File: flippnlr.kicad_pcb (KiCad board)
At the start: 2 copper layers, 87 parts, among them J1 Pwr In, J2 TP3, J3 TP1, J4 Opt Out, J5 Opt Out, J6 Data Out, J7 Data In, J8 TP2, U1 LD1117 3.3V, U10 TPL7407LA, U11 TPL7407LA, U12 TPL7407LA, U13 SN74HCS365, U2 SN74HCS594, U3 SN74HCS594, U4 SN74HCS594, U5 SN74HCS594, U6 SN74HCS594, U7 TPL7407LA, U8 TPL7407LA, U9 TPL7407LA

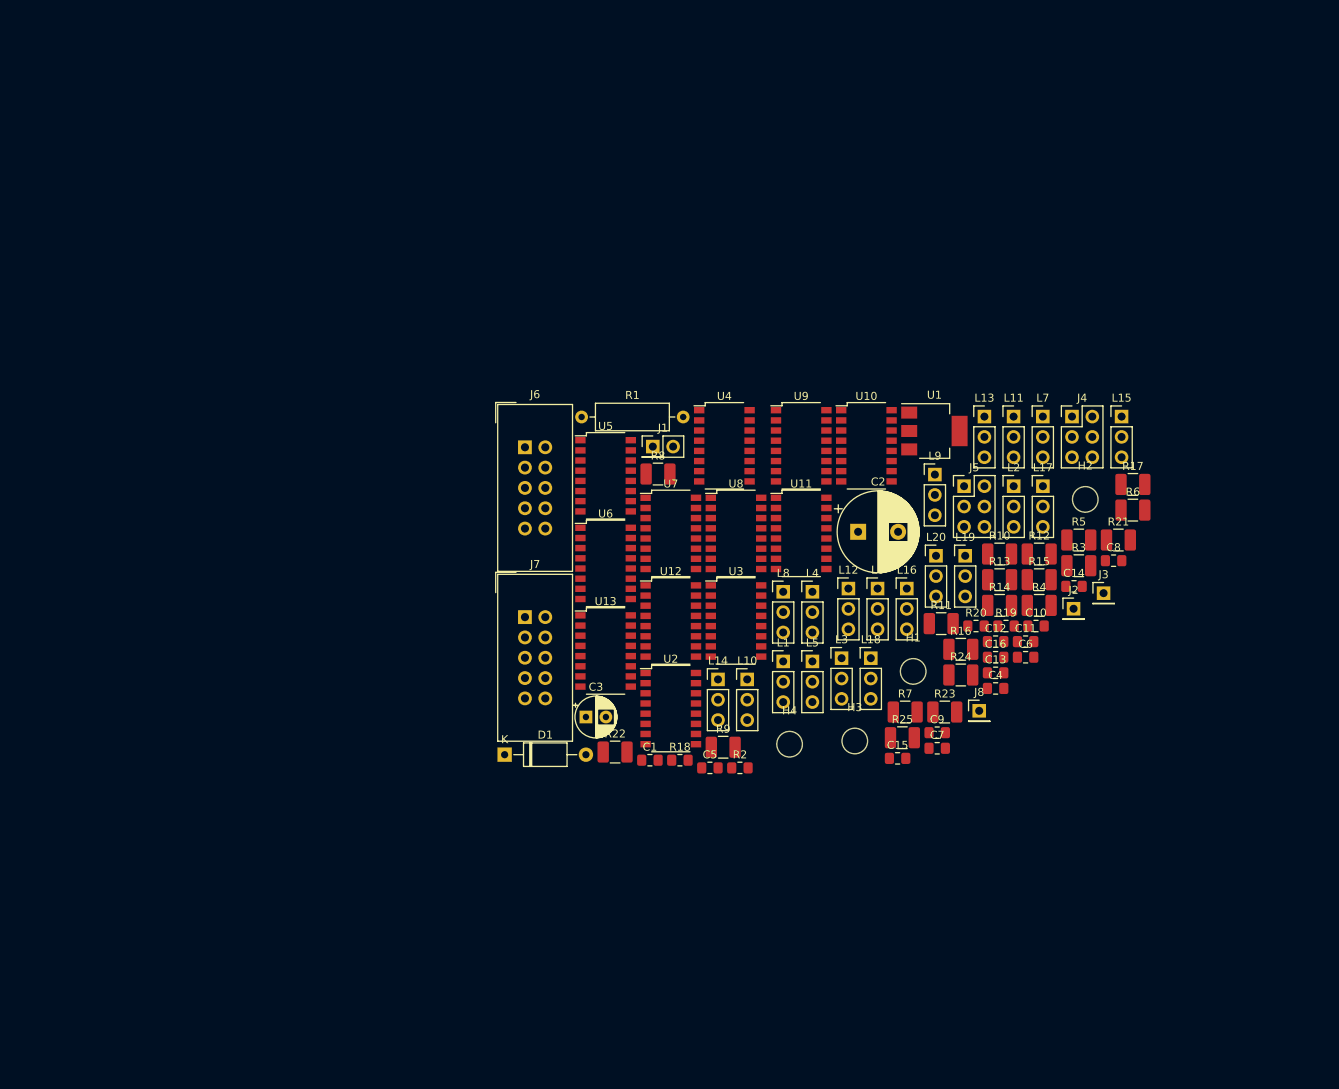
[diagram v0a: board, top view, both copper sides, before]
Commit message: fix kicad lib path and begin layout
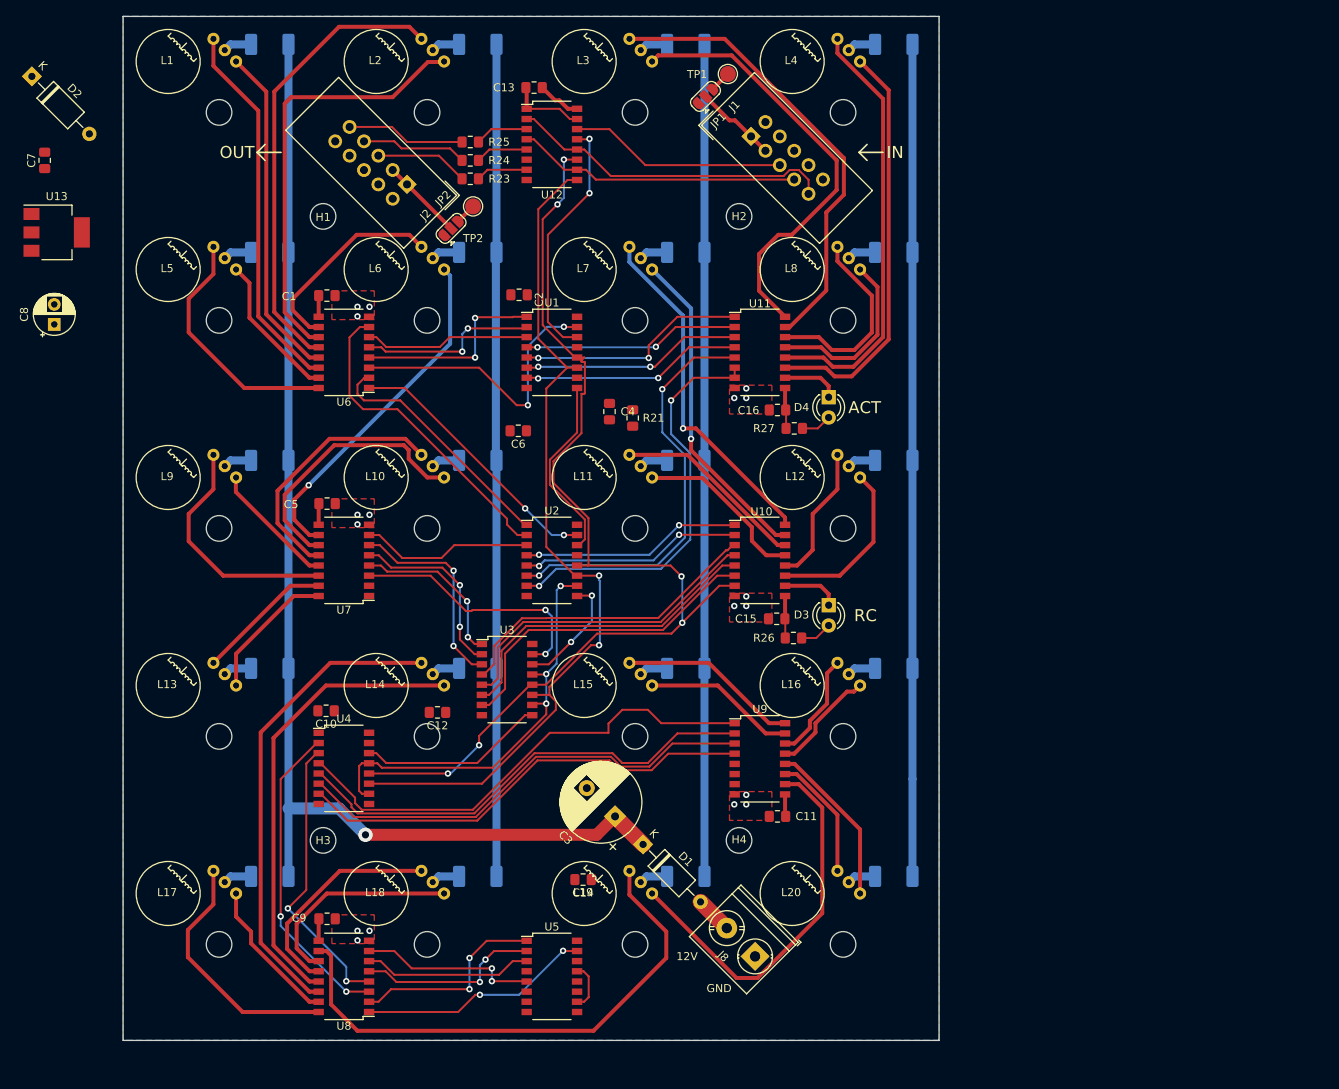
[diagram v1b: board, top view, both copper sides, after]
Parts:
- removed J3: TP1, Connector_PinHeader_2.54mm:PinHeader_1x01_P2.54mm_Vertical
- removed J4, J5: Opt Out, Connector_PinHeader_2.54mm:PinHeader_2x03_P2.54mm_Vertical
- removed J6: Data Out, Connector_IDC:IDC-Header_2x05_P2.54mm_Vertical
- removed J7: Data In, Connector_IDC:IDC-Header_2x05_P2.54mm_Vertical
- removed R22: TBA, Resistor_SMD:R_1210_3225Metric_Pad1.42x2.65mm_HandSolder
- added D2: 1n5817, Diode_THT:D_A-405_P10.16mm_Horizontal, F.Cu at (38.6, 35.5)
- added D3: 3GWY4, LED_THT:LED_D3.0mm, F.Cu at (138.2, 101.6)
- added D4: 3GWY4, LED_THT:LED_D3.0mm, F.Cu at (138.2, 75.6)
- added JP1: PWR, Jumper:SolderJumper-3_P1.3mm_Open_RoundedPad1.0x1.5mm, F.Cu at (122.8, 38.0)
- added JP2: PWR, Jumper:SolderJumper-3_P1.3mm_Open_RoundedPad1.0x1.5mm, F.Cu at (91.0, 54.5)
- added R26: 4k7, Resistor_SMD:R_0805_2012Metric_Pad1.15x1.40mm_HandSolder, F.Cu at (133.8, 105.7)
- added R27: 4k7, Resistor_SMD:R_0805_2012Metric_Pad1.15x1.40mm_HandSolder, F.Cu at (133.9, 79.5)
- added TP1: PWR, TestPoint:TestPoint_Pad_D2.0mm, F.Cu at (125.6, 35.2)
- added TP2: PWR, TestPoint:TestPoint_Pad_D2.0mm, F.Cu at (93.8, 51.8)
- C2: value 470uF -> 100nF; footprint Capacitor_THT:CP_Radial_D10.0mm_P5.00mm -> Capacitor_SMD:C_0805_2012Metric_Pad1.15x1.40mm_HandSolder
- C3: value 10uF -> 470uF; footprint Capacitor_THT:CP_Radial_D5.0mm_P2.50mm -> Capacitor_THT:CP_Radial_D10.0mm_P5.00mm
- C8: value 100nF -> 10uF; footprint Capacitor_SMD:C_0805_2012Metric_Pad1.15x1.40mm_HandSolder -> Capacitor_THT:CP_Radial_D5.0mm_P2.50mm
- D1: value 1n4001 -> 1n5817
- J1: value Pwr In -> Data In; footprint Connector_PinHeader_2.54mm:PinHeader_2x01_P2.54mm_Vertical -> Connector_IDC:IDC-Header_2x05_P2.54mm_Vertical
- J2: value TP3 -> Data Out; footprint Connector_PinHeader_2.54mm:PinHeader_1x01_P2.54mm_Vertical -> Connector_IDC:IDC-Header_2x05_P2.54mm_Vertical
- J8: value TP2 -> 12V; footprint Connector_PinHeader_2.54mm:PinHeader_1x01_P2.54mm_Vertical -> TerminalBlock_Phoenix:TerminalBlock_Phoenix_PT-1,5-2-5.0-H_1x02_P5.00mm_Horizontal
- L1, L10, L11, L12, L13, L14, L15, L16, L17, L18, L19, L2, L20, L3, L4, L5, L6, L7, L8, L9: footprint Connector_PinHeader_2.54mm:PinHeader_1x03_P2.54mm_Vertical -> flipdot:Flipdot
- R1: value 2.7 -> 62; footprint Resistor_THT:R_Axial_DIN0309_L9.0mm_D3.2mm_P12.70mm_Horizontal -> Resistor_SMD:R_2010_5025Metric_Pad1.52x2.65mm_HandSolder; moved to B.Cu
- R10, R11, R12, R13, R14, R15, R16, R17, R3, R4, R5, R6, R7, R8, R9: value TBA -> 62; footprint Resistor_SMD:R_1210_3225Metric_Pad1.42x2.65mm_HandSolder -> Resistor_SMD:R_2010_5025Metric_Pad1.52x2.65mm_HandSolder; moved to B.Cu
- R18, R19, R20: value 33 -> 62; footprint Resistor_SMD:R_0805_2012Metric_Pad1.15x1.40mm_HandSolder -> Resistor_SMD:R_2010_5025Metric_Pad1.52x2.65mm_HandSolder; moved to B.Cu
- R2: value 1k -> 62; footprint Resistor_SMD:R_0805_2012Metric_Pad1.15x1.40mm_HandSolder -> Resistor_SMD:R_2010_5025Metric_Pad1.52x2.65mm_HandSolder; moved to B.Cu
- R21: value TBA -> 1k; footprint Resistor_SMD:R_1210_3225Metric_Pad1.42x2.65mm_HandSolder -> Resistor_SMD:R_0805_2012Metric_Pad1.15x1.40mm_HandSolder
- R23, R24, R25: value TBA -> 33; footprint Resistor_SMD:R_1210_3225Metric_Pad1.42x2.65mm_HandSolder -> Resistor_SMD:R_0805_2012Metric_Pad1.15x1.40mm_HandSolder
- U1: value LD1117 3.3V -> SN74HCS594; footprint Package_TO_SOT_SMD:SOT-223-3_TabPin2 -> Package_SO:SOP-16_4.4x10.4mm_P1.27mm
- U12: value TPL7407LA -> SN74HCS365
- U13: value SN74HCS365 -> LD1117 3.3V; footprint Package_SO:SOP-16_4.4x10.4mm_P1.27mm -> Package_TO_SOT_SMD:SOT-223-3_TabPin2
- U6: value SN74HCS594 -> TPL7407LA
- moved C8 135.7 mm to (41.4, 66.5), turned to 90 degrees
- moved C7 133.6 mm to (40.2, 46.0), turned to 90 degrees
- moved R17 118.5 mm to (68.3, 135.5)
- moved L17 117.8 mm to (62.0, 144.0), turned to 315 degrees
- moved R5 107.3 mm to (68.3, 57.5)
- moved L13 103.7 mm to (62.0, 118.0), turned to 315 degrees
- moved J2 98.8 mm to (85.5, 49.0), turned to 225 degrees
- moved L1 98.4 mm to (62.0, 40.0), turned to 315 degrees
- moved R2 96.2 mm to (94.3, 31.5)
- moved C13 93.2 mm to (101.4, 36.9), turned to 180 degrees
- moved H1 93.1 mm to (75.0, 53.0)
- moved R25 92.0 mm to (93.4, 43.7)
- moved R13 91.9 mm to (68.3, 109.5)
- moved L9 89.7 mm to (62.0, 92.0), turned to 315 degrees
- moved C10 89.4 mm to (75.4, 114.8), turned to 180 degrees
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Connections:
- C1 pad 1: +10V -> +12V
- C10 pad 1: +12V -> +3V3
- C12 pad 1: +12V -> +3V3
- C13 pad 1: +12V -> +3V3
- C14 pad 1: +12V -> +3V3
- C16 pad 1: +3V3 -> +12V
- C2 pad 1: +12V -> +3V3
- C3 pad 1: +3V3 -> +12V
- C4 pad 1: +3V3 -> GND
- C4 pad 2: GND -> RST
- C5 pad 1: +3V3 -> +12V
- C7 pad 1: +3V3 -> +10V
- C9 pad 1: GND -> +12V
- C9 pad 2: RST -> GND
- D1 pad 1: +10V -> +12V
- D1 pad 2: +12V -> Net-(D1-Pad2)
- J8 pad 1: Net-(J5-Pad2) -> GND
- L10 pad 1: S17 -> S9
- L10 pad 3: C17 -> C9
- L11 pad 1: S2 -> S10
- L11 pad 3: C2 -> C10
- L12 pad 1: S6 -> S11
- L12 pad 3: C6 -> C11
- L13 pad 1: S10 -> S12
- L13 pad 3: C10 -> C12
- L14 pad 1: S14 -> S13
- L14 pad 3: C14 -> C13
- L15 pad 1: S18 -> S14
- L15 pad 3: C18 -> C14
- L16 pad 1: S3 -> S15
- L16 pad 3: C3 -> C15
- L17 pad 1: S7 -> S16
- L17 pad 3: C7 -> C16
- L18 pad 1: S11 -> S17
- L18 pad 3: C11 -> C17
- L19 pad 1: S15 -> S18
- L19 pad 3: C15 -> C18
- L2 pad 1: S4 -> S1
- L2 pad 3: C4 -> C1
- L3 pad 1: S8 -> S2
- L3 pad 3: C8 -> C2
- L4 pad 1: S12 -> S3
- L4 pad 3: C12 -> C3
- L5 pad 1: S16 -> S4
- L5 pad 3: C16 -> C4
- L6 pad 1: S1 -> S5
- L6 pad 3: C1 -> C5
- L7 pad 1: S5 -> S6
- L7 pad 3: C5 -> C6
- L8 pad 1: S9 -> S7
- L8 pad 3: C9 -> C7
- L9 pad 1: S13 -> S8
- L9 pad 3: C13 -> C8
- R1 pad 1: +12V -> Net-(L1-Pad2)
- R1 pad 2: Net-(J1-Pad1) -> +12V
- R10 pad 1: Net-(L8-Pad2) -> Net-(L10-Pad2)
- R11 pad 1: Net-(L9-Pad2) -> Net-(L11-Pad2)
- R12 pad 1: Net-(L10-Pad2) -> Net-(L12-Pad2)
- R13 pad 1: Net-(L11-Pad2) -> Net-(L13-Pad2)
- R14 pad 1: Net-(L12-Pad2) -> Net-(L14-Pad2)
- R15 pad 1: Net-(L13-Pad2) -> Net-(L15-Pad2)
- R16 pad 1: Net-(L14-Pad2) -> Net-(L16-Pad2)
- R17 pad 1: Net-(L15-Pad2) -> Net-(L17-Pad2)
- R18 pad 1: DOUT -> Net-(L18-Pad2)
- R18 pad 2: Net-(R18-Pad2) -> +12V
- R19 pad 1: DCOUT -> Net-(L19-Pad2)
- R19 pad 2: Net-(R19-Pad2) -> +12V
- R2 pad 1: +3V3 -> Net-(L2-Pad2)
- R2 pad 2: RST -> +12V
- R20 pad 1: RCOUT -> Net-(L20-Pad2)
- R20 pad 2: Net-(R20-Pad2) -> +12V
- R21 pad 1: Net-(L16-Pad2) -> +3V3
- R21 pad 2: +12V -> RST
- R23 pad 1: Net-(L18-Pad2) -> DOUT
- R23 pad 2: +12V -> Net-(R23-Pad2)
- R24 pad 1: Net-(L19-Pad2) -> DCOUT
- R24 pad 2: +12V -> Net-(R24-Pad2)
- R25 pad 1: Net-(L20-Pad2) -> RCOUT
- R25 pad 2: +12V -> Net-(R25-Pad2)
- R3 pad 1: Net-(L1-Pad2) -> Net-(L3-Pad2)
- R4 pad 1: Net-(L2-Pad2) -> Net-(L4-Pad2)
- R5 pad 1: Net-(L3-Pad2) -> Net-(L5-Pad2)
- R6 pad 1: Net-(L4-Pad2) -> Net-(L6-Pad2)
- R7 pad 1: Net-(L5-Pad2) -> Net-(L7-Pad2)
- R8 pad 1: Net-(L6-Pad2) -> Net-(L8-Pad2)
- R9 pad 1: Net-(L7-Pad2) -> Net-(L9-Pad2)
- U1 pad 1: GND -> LC0
- U1 pad 2: +3V3 -> LS1
- U1 pad 3: +10V -> LC1
- U10 pad 1: Net-(U10-Pad1) -> LS6
- U10 pad 10: S10 -> Net-(D3-Pad1)
- U10 pad 11: C9 -> C11
- U10 pad 12: S9 -> S11
- U10 pad 13: C8 -> C10
- U10 pad 14: S8 -> S10
- U10 pad 15: C7 -> C6
- U10 pad 16: S7 -> S6
- U10 pad 2: Net-(U10-Pad2) -> LC6
- U10 pad 3: Net-(U10-Pad3) -> LS10
- U10 pad 4: Net-(U10-Pad4) -> LC10
- U10 pad 5: Net-(U10-Pad5) -> LS11
- U10 pad 6: Net-(U10-Pad6) -> LC11
- U10 pad 7: Net-(U10-Pad7) -> RC
- U11 pad 1: Net-(U11-Pad1) -> LC2
- U11 pad 10: C13 -> Net-(D4-Pad1)
- U11 pad 11: S13 -> C3
- U11 pad 12: C12 -> S3
- U11 pad 13: S12 -> C7
- U11 pad 14: C11 -> S7
- U11 pad 15: S11 -> S2
- U11 pad 16: C10 -> C2
- U11 pad 2: Net-(U11-Pad2) -> LS2
- U11 pad 3: Net-(U11-Pad3) -> LS3
- U11 pad 4: Net-(U11-Pad4) -> LC3
- U11 pad 5: Net-(U11-Pad5) -> LS7
- U11 pad 6: Net-(U11-Pad6) -> LC7
- U11 pad 7: Net-(U11-Pad7) -> LC7
- U12 pad 1: Net-(U12-Pad1) -> GND
- U12 pad 10: S17 -> DCIN
- U12 pad 11: C16 -> RC
- U12 pad 12: S16 -> RCIN
- U12 pad 13: C15 -> D0
- U12 pad 14: S15 -> DIN
- U12 pad 15: C14 -> GND
- U12 pad 16: S14 -> +3V3
- U12 pad 2: Net-(U12-Pad2) -> RCIN
- U12 pad 3: Net-(U12-Pad3) -> Net-(R25-Pad2)
- U12 pad 4: Net-(U12-Pad4) -> DCIN
- U12 pad 5: Net-(U12-Pad5) -> Net-(R24-Pad2)
- U12 pad 6: Net-(U12-Pad6) -> D40
- U12 pad 7: Net-(U12-Pad7) -> Net-(R23-Pad2)
- U12 pad 9: +12V -> DC
- U13 pad 2: DIN -> +3V3
- U13 pad 3: D0 -> +10V
- U2 pad 1: Net-(U2-Pad1) -> LC4
- U2 pad 14: D0 -> D8
- U2 pad 15: Net-(U2-Pad15) -> LS4
- U2 pad 2: Net-(U2-Pad2) -> LS5
- U2 pad 3: Net-(U2-Pad3) -> LC5
- U2 pad 4: Net-(U2-Pad4) -> LS6
- U2 pad 5: Net-(U2-Pad5) -> LC6
- U2 pad 6: Net-(U2-Pad6) -> LS7
- U2 pad 7: Net-(U2-Pad7) -> LC7
- U2 pad 9: D8 -> D16
- U3 pad 1: Net-(U3-Pad1) -> LC8
- U3 pad 14: D8 -> D16
- U3 pad 15: Net-(U3-Pad15) -> LS8
- U3 pad 2: Net-(U3-Pad2) -> LS9
- U3 pad 3: Net-(U3-Pad3) -> LC9
- U3 pad 4: Net-(U3-Pad4) -> LS10
- U3 pad 5: Net-(U3-Pad5) -> LC10
- U3 pad 6: Net-(U10-Pad1) -> LS11
- U3 pad 7: Net-(U10-Pad2) -> LC11
- U3 pad 9: D16 -> D24
- U4 pad 1: Net-(U10-Pad4) -> LC12
- U4 pad 14: D16 -> D24
- U4 pad 15: Net-(U10-Pad3) -> LS12
- U4 pad 2: Net-(U10-Pad5) -> LS13
- U4 pad 3: Net-(U10-Pad6) -> LC13
- U4 pad 4: Net-(U10-Pad7) -> LS14
- U4 pad 5: Net-(U11-Pad1) -> LC14
- U4 pad 6: Net-(U11-Pad2) -> LS15
- U4 pad 7: Net-(U11-Pad3) -> LC15
- U4 pad 9: D24 -> D32
- U5 pad 1: Net-(U11-Pad5) -> LC16
- U5 pad 14: D24 -> D32
- U5 pad 15: Net-(U11-Pad4) -> LS16
- U5 pad 2: Net-(U11-Pad6) -> LS17
- U5 pad 3: Net-(U11-Pad7) -> LC17
- U5 pad 4: Net-(U12-Pad1) -> LC18
- U5 pad 5: Net-(U12-Pad2) -> LS18
- U5 pad 6: Net-(U12-Pad3) -> LS19
- U5 pad 7: Net-(U12-Pad4) -> LC19
- U5 pad 9: D32 -> D40
- U6 pad 1: Net-(U12-Pad6) -> LS4
- U6 pad 10: RST -> S5
- U6 pad 11: DC -> C1
- U6 pad 12: RC -> S1
- U6 pad 13: RST -> C0
- U6 pad 14: D32 -> S0
- U6 pad 15: Net-(U12-Pad5) -> C4
- U6 pad 16: +3V3 -> S4
- U6 pad 2: Net-(U12-Pad7) -> LC4
- U6 pad 3: Net-(U6-Pad3) -> LS0
- U6 pad 4: Net-(U6-Pad4) -> LC0
- U6 pad 5: Net-(U6-Pad5) -> LS1
- U6 pad 6: Net-(U6-Pad6) -> LC1
- U6 pad 7: Net-(U6-Pad7) -> LS5
- U6 pad 9: D40 -> +12V
- U7 pad 1: Net-(U2-Pad15) -> LC12
- U7 pad 10: S3 -> C5
- U7 pad 11: C2 -> C9
- U7 pad 12: S2 -> S9
- U7 pad 13: C1 -> C8
- U7 pad 14: S1 -> S8
- U7 pad 15: C0 -> S12
- U7 pad 16: S0 -> C12
- U7 pad 2: Net-(U2-Pad1) -> LS12
- U7 pad 3: Net-(U2-Pad2) -> LS8
- U7 pad 4: Net-(U2-Pad3) -> LC8
- U7 pad 5: Net-(U2-Pad4) -> LS9
- U7 pad 6: Net-(U2-Pad5) -> LC9
- U7 pad 7: Net-(U2-Pad6) -> LC5
- U8 pad 1: Net-(U6-Pad3) -> LS16
- U8 pad 10: Net-(U8-Pad10) -> S18
- U8 pad 11: Net-(U8-Pad11) -> C17
- U8 pad 12: C19 -> S17
- U8 pad 13: S19 -> C13
- U8 pad 14: C18 -> S13
- U8 pad 15: S18 -> C16
- U8 pad 16: C17 -> S16
- U8 pad 2: Net-(U6-Pad4) -> LC16
- U8 pad 3: Net-(U6-Pad5) -> LS13
- U8 pad 4: Net-(U6-Pad6) -> LC13
- U8 pad 5: Net-(U6-Pad7) -> LS17
- U8 pad 6: Net-(U8-Pad6) -> LC17
- U8 pad 7: Net-(U8-Pad7) -> LS18
- U9 pad 1: Net-(U2-Pad7) -> LS14
- U9 pad 10: C6 -> C18
- U9 pad 11: S6 -> S19
- U9 pad 12: C5 -> C19
- U9 pad 13: S5 -> C15
- U9 pad 14: C4 -> S15
- U9 pad 15: S4 -> C14
- U9 pad 16: C3 -> S14
- U9 pad 2: Net-(U3-Pad15) -> LC14
- U9 pad 3: Net-(U3-Pad1) -> LS15
- U9 pad 4: Net-(U3-Pad2) -> LC15
- U9 pad 5: Net-(U3-Pad3) -> LC19
- U9 pad 6: Net-(U3-Pad4) -> LS19
- U9 pad 7: Net-(U3-Pad5) -> LC18
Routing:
- net +12V: track 0.00 -> 485.1 mm, vias 0 -> 1
- net RC: track 0.00 -> 136.4 mm, vias 0 -> 6
- net DC: track 0.00 -> 110.1 mm, vias 0 -> 2
- net S18: track 0.00 -> 67.7 mm
- net LS14: track 0.00 -> 61.3 mm
- net S13: track 0.00 -> 59.8 mm
- net RST: track 0.00 -> 59.7 mm, vias 0 -> 3
- net LC14: track 0.00 -> 59.4 mm
- net LS15: track 0.00 -> 58.5 mm
- net LC15: track 0.00 -> 57.9 mm
- net C13: track 0.00 -> 57.5 mm
- net S2: track 0.00 -> 57.5 mm
- net S1: track 0.00 -> 57.3 mm
- net C2: track 0.00 -> 54.7 mm
- net S3: track 0.00 -> 53.9 mm
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- added copper zone on B.Cu, net GND
- added copper zone on F.Cu, net GND
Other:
- board outline added: 102 x 128 mm
- net class Default: trace_width 0.25 -> 0.2
- net class metrico added: clearance 0.2, trace_width 0.2, via_dia 0.6858, via_drill 0.3302
- rule pad_to_mask_clearance: 0 -> 0.0508
- rule trace_min: 0.2 -> 0.1524
- rule via_min_drill: 0.3 -> 0.3302
- rule via_min_size: 0.4 -> 0.6858
- board text added: "12V"
- board text added: "ACT"
- board text added: "GND"
- board text added: "IN"
- board text added: "OUT"
- board text added: "RC"

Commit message: reroute signals slightly
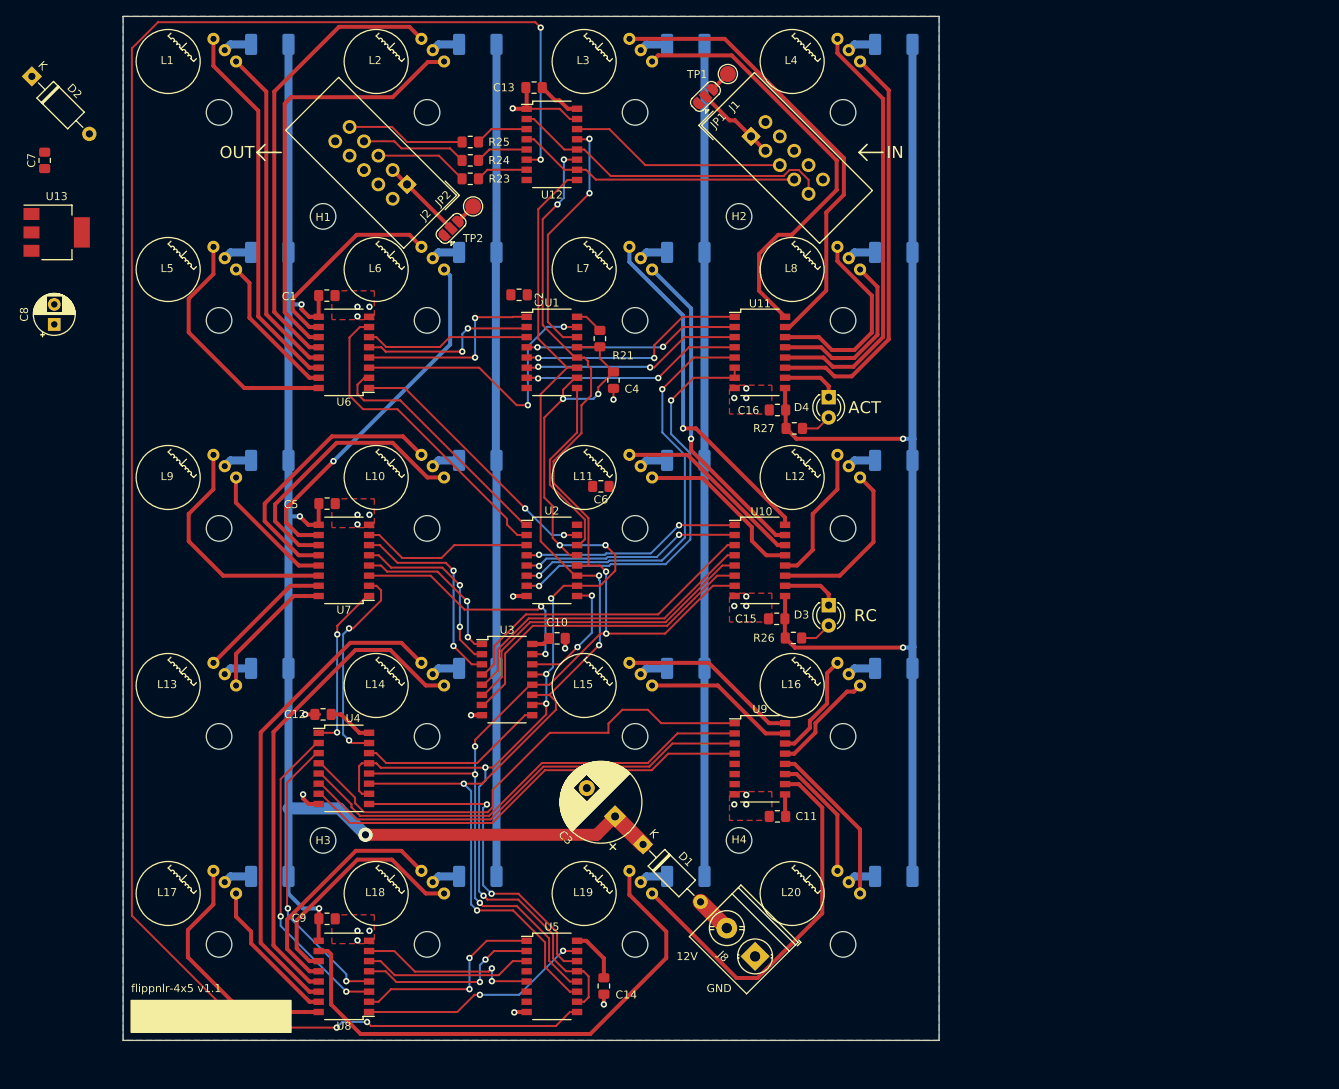
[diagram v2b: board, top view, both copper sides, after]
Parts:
- moved C10 30.3 mm to (104.2, 105.8), turned to 0 degrees
- moved C12 14.3 mm to (75.0, 115.2)
- moved C14 13.6 mm to (110.1, 149.2), turned to 270 degrees
- moved C6 12.4 mm to (109.7, 86.8)
- moved R21 10.7 mm to (109.6, 68.3), turned to 270 degrees
- moved C4 3.96 mm to (111.3, 73.5), turned to 90 degrees
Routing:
- net D40: track 0.00 -> 242.1 mm, vias 0 -> 4
- net RST: track 59.7 -> 149.8 mm, vias 3 -> 9
- net +12V: track 485.1 -> 534.9 mm, vias 1 -> 6
- net D32: track 0.00 -> 42.3 mm, vias 0 -> 2
- net DC: track 110.1 -> 145.2 mm, vias 2 -> 4
- net RC: track 136.4 -> 164.7 mm, vias 6 -> 7
- net LS12: track 0.00 -> 25.7 mm, vias 0 -> 2
- net LC12: track 0.00 -> 21.2 mm, vias 0 -> 2
- net +3V3: track 5.45 -> 23.7 mm
- net GND: track 9.52 -> 24.4 mm, vias 18 -> 27
- net C13: track 57.5 -> 61.6 mm
- net C17: track 26.5 -> 30.2 mm
- net S17: track 27.8 -> 30.2 mm
- net S9: track 32.4 -> 34.7 mm
- net S13: track 59.8 -> 61.9 mm
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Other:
- board text added: "flippnlr-4x5 v1.1"

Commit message: pcb roughly routed
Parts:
- moved D2 91.6 mm to (102.7, 101.0)
- moved C8 72.6 mm to (111.9, 84.0)
- moved U13 68.3 mm to (105.8, 78.6), turned to 315 degrees
- moved C7 67.3 mm to (101.7, 73.5), turned to 0 degrees
- moved C2 58.2 mm to (157.3, 69.5), turned to 90 degrees
- moved R21 49.6 mm to (158.7, 75.5)
- moved R19 49.5 mm to (169.7, 139.2), turned to 90 degrees
- moved JP1 48.2 mm to (170.8, 42.0)
- moved C1 48.2 mm to (123.5, 66.9)
- moved C10 48.2 mm to (152.2, 109.8)
- moved C11 48.2 mm to (179.8, 132.0)
- moved C12 48.2 mm to (123.0, 119.2)
- moved C13 48.2 mm to (149.4, 40.9)
- moved C15 48.2 mm to (179.7, 107.3)
- moved C16 48.2 mm to (179.8, 81.2)
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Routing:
- net +3V3: track 23.7 -> 265.5 mm, vias 0 -> 10
- net +12V: track 534.9 -> 590.8 mm, vias 6 -> 10
- net LC19: track 0.00 -> 44.5 mm, vias 0 -> 2
- net LS19: track 0.00 -> 44.4 mm, vias 0 -> 2
- net LC18: track 0.00 -> 42.3 mm, vias 0 -> 2
- net +10V: track 0.00 -> 30.1 mm
- net GND: track 24.4 -> 33.4 mm, vias 27 -> 32
- net DC: track 145.2 -> 152.7 mm
- net Net-(D1-Pad2): track 4.64 -> 10.3 mm
- net Net-(L19-Pad2): track 3.59 -> 8.17 mm
- net LC7: track 51.6 -> 55.4 mm
- net LS7: track 52.2 -> 55.9 mm
- net LS16: track 29.2 -> 32.9 mm
- net RST: track 149.8 -> 147.1 mm, vias 9 -> 8
- net LS15: track 57.8 -> 60.4 mm
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- added copper zone on F.Cu, net +3V3

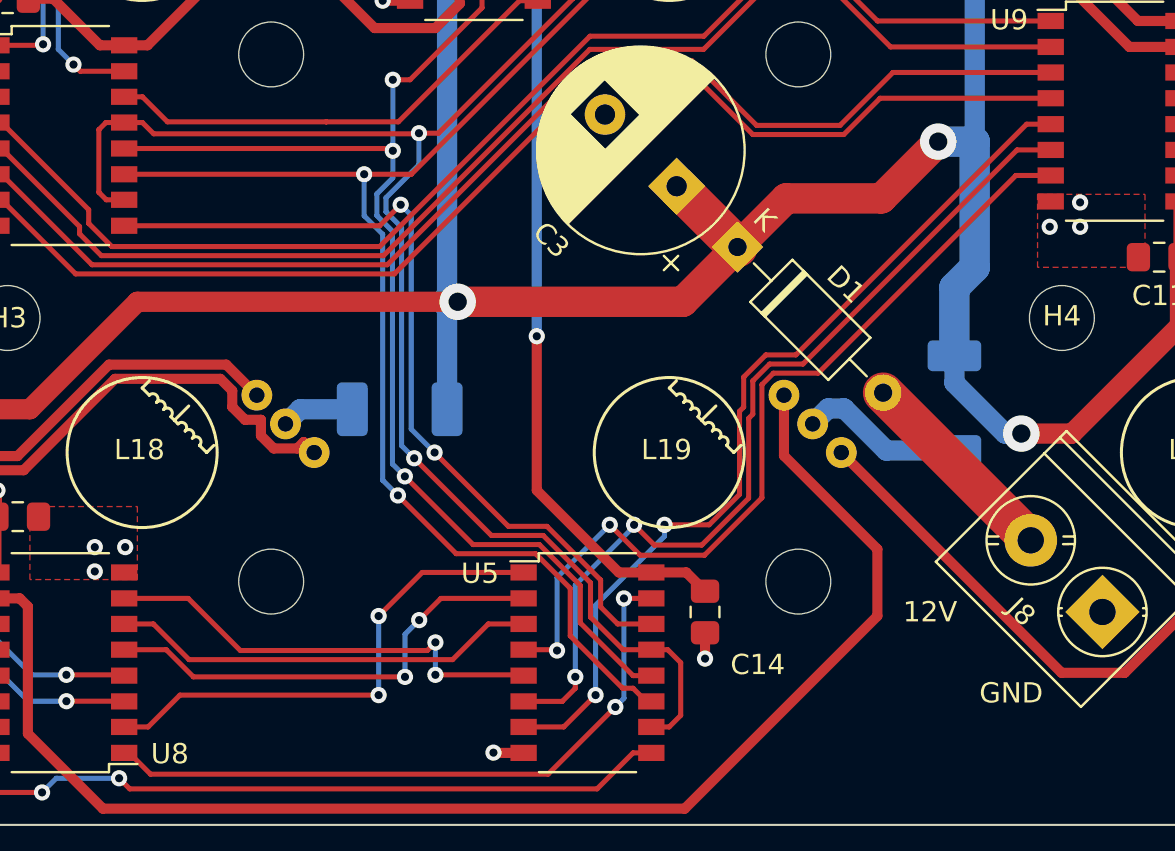
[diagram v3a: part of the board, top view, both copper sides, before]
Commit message: correct mis-wired U5
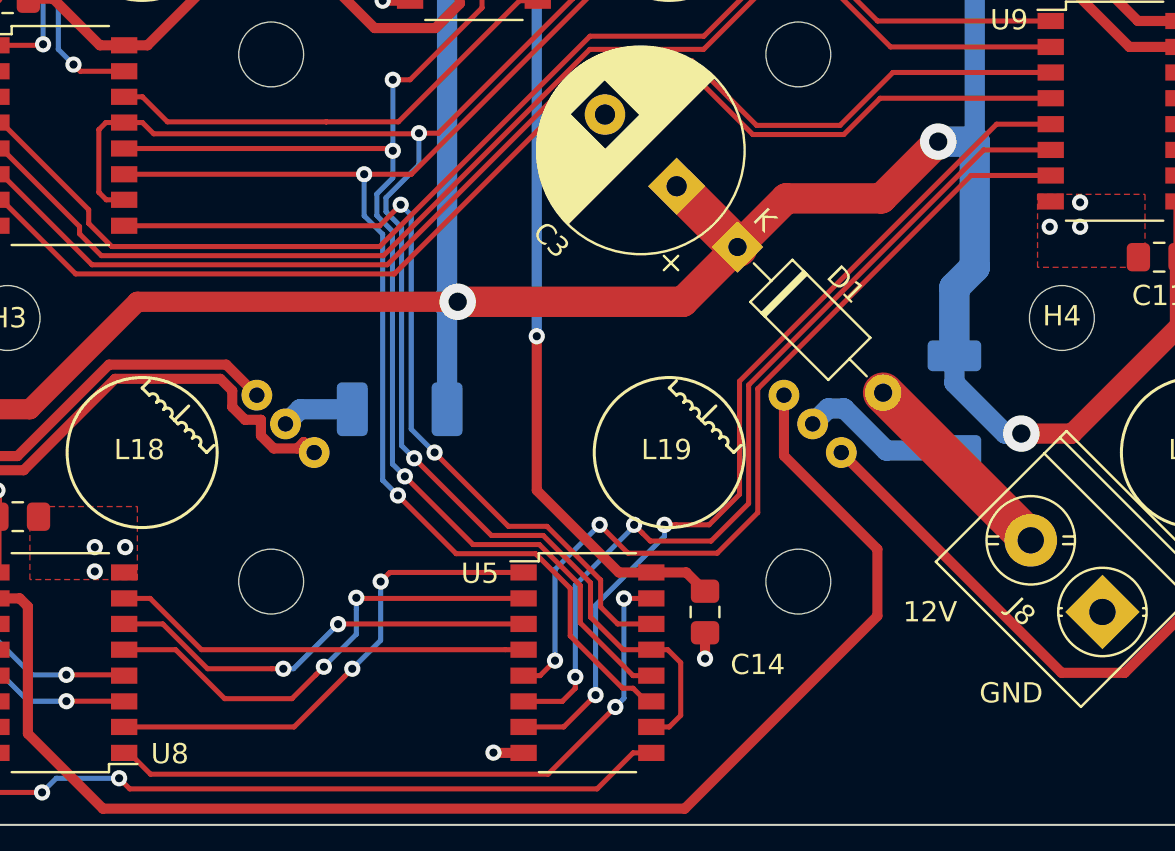
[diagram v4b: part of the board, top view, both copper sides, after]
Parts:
- R23, R24, R25: value 33 -> 220
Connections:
- U5 pad 4: LC18 -> LS18
- U5 pad 5: LS18 -> LC18
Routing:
- net LS18: track 22.5 -> 20.7 mm, vias 2 -> 0
- net LC18: track 42.3 -> 43.6 mm
- net LS17: track 23.1 -> 23.8 mm
- net LC16: track 25.1 -> 24.6 mm
- net LC17: track 21.2 -> 21.5 mm, vias 0 -> 2
